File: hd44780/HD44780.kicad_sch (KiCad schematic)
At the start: 3 parts

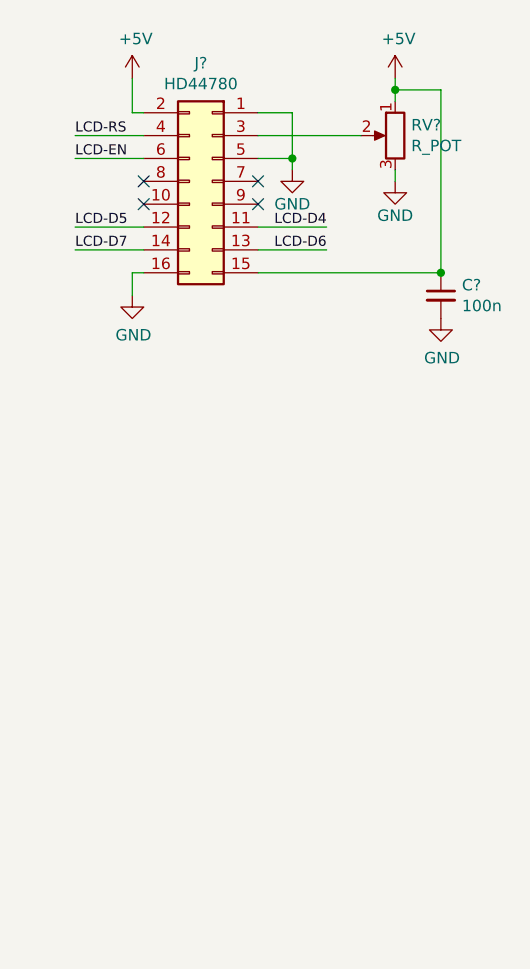
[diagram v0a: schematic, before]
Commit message: Add Inline connector type
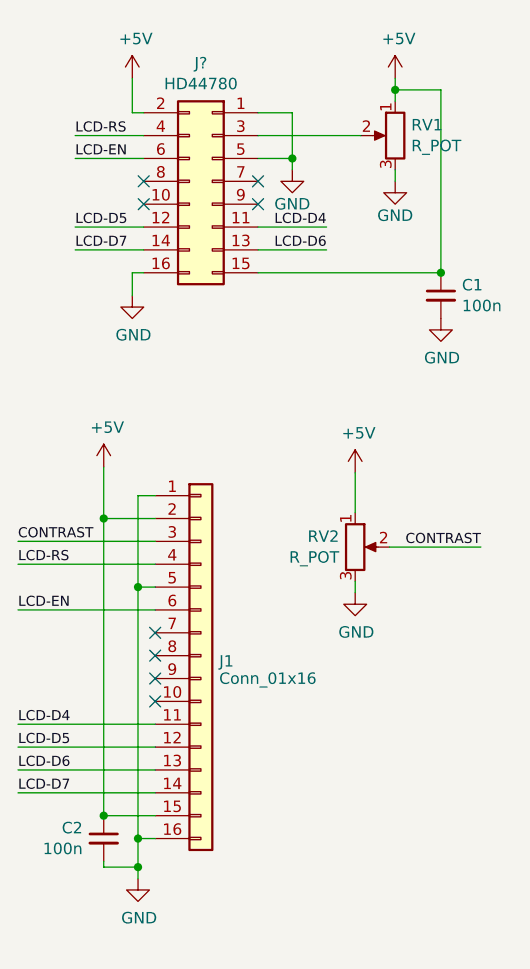
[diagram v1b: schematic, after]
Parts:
- removed C?: 100n, symbol Device:C_Small
- removed RV?: R_POT, symbol Device:R_POT
- added C1, C2: 100n, symbol Device:C_Small
- added J1: Conn_01x16, symbol Connector_Generic:Conn_01x16
- added RV1, RV2: R_POT, symbol Device:R_POT
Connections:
- net +5V: now also C1.1, C2.1, J1.15 (Pin_15), J1.2 (Pin_2), RV1.1, RV2.1
- net GND: now also C1.2, C2.2, J1.1 (Pin_1), J1.16 (Pin_16), J1.5 (Pin_5), RV1.3, RV2.3
- net LCD-D4: now also J1.11 (Pin_11)
- net LCD-D5: now also J1.12 (Pin_12)
- net LCD-D6: now also J1.13 (Pin_13)
- net LCD-D7: now also J1.14 (Pin_14)
- net LCD-EN: now also J1.6 (Pin_6)
- net LCD-RS: now also J1.4 (Pin_4)
- net at J?.3 (Pin_3): now also RV1.2
- new net CONTRAST: J1.3 (Pin_3), RV2.2
- no-connect marks 4 -> 8

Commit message: Fix grid alignment and update to KiCad 9
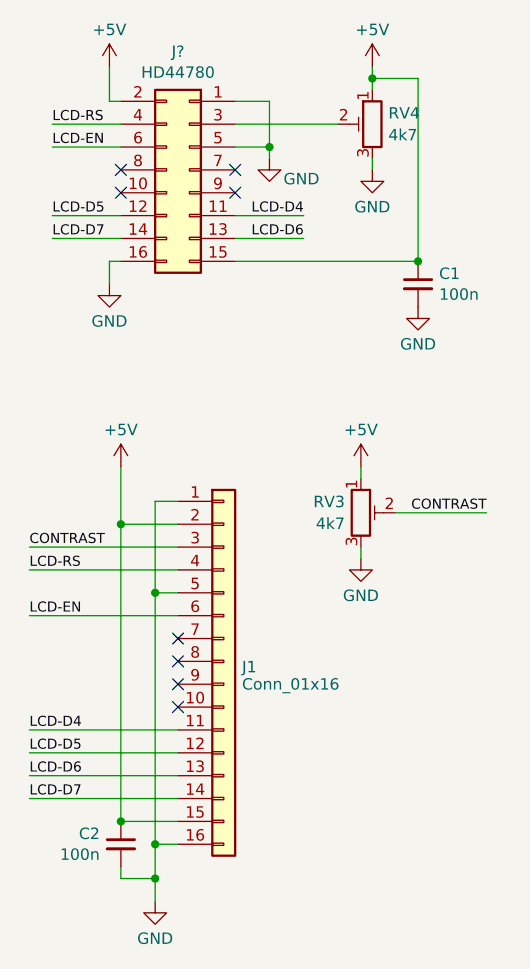
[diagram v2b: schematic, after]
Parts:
- removed RV1, RV2: R_POT, symbol Device:R_POT
- added RV3, RV4: 4k7, symbol Device:R_Potentiometer_Trim
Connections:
- net +5V: now also RV3.1, RV4.1
- net CONTRAST: now also RV3.2
- net GND: now also RV3.3, RV4.3
- net at J?.3 (Pin_3): now also RV4.2
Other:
- moved on the sheet: C1, C2, J1, J?
